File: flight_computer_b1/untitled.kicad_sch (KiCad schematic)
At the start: 1 part, among them U12 LTC7810

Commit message: WIP
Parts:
- added C12: C, symbol Device:C
- added C13: 1.2u, symbol Device:C
- added R59: 931k, symbol Device:R
- added R60: 10k, symbol Device:R
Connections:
- net V_in: now reaches U12.32 (RUN1)
- net at U12.45 (TRACK/SS1): now also C13.1
- net VFB1: now reaches U12.47 (VFB1)
- net VFB1: now also C12.2, R59.1, R60.2
- net GND: now reaches U12.9 (OVLO)
- net GND: now also C13.2, R60.1
- new net: C12.1, R59.2

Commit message: vers1
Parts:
- added C14, C15, C16, C17, C18: C, symbol Device:C
- added L2: L, symbol Device:L
- added Q3, Q4: NMOS, symbol Simulation_SPICE:NMOS
- added R62, R63: R, symbol Device:R
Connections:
- net GND: now also U12.10 (NDRV), U12.25 (PGND), U12.4 (PLLIN/SPREAD), U12.49 (SGND), U12.5 (SGND), U12.7 (REGSD), U12.8 (MODE), C16.2, C17.2, C18.1, Q4.1 (D)
- net V_in: now also C16.1, Q3.3 (S)
- net V_out: now reaches U12.1 (SENSE1-)
- net V_out: now also C15.2, C17.1, L2.1, R63.2
- net at U12.26 (DRVcc): now also C18.2
- net at U12.37 (BG1): now also Q4.2 (G)
- net at U12.40 (BOOST1): now also C14.2
- net at U12.41 (SW1): now also C14.1, L2.2, Q3.1 (D), Q4.3 (S), R62.1
- net at U12.42 (TG1): now also Q3.2 (G)
- net at U12.48 (SENSE1+): now also C15.1, R62.2, R63.1
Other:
- moved on the sheet: C12, R59, R60

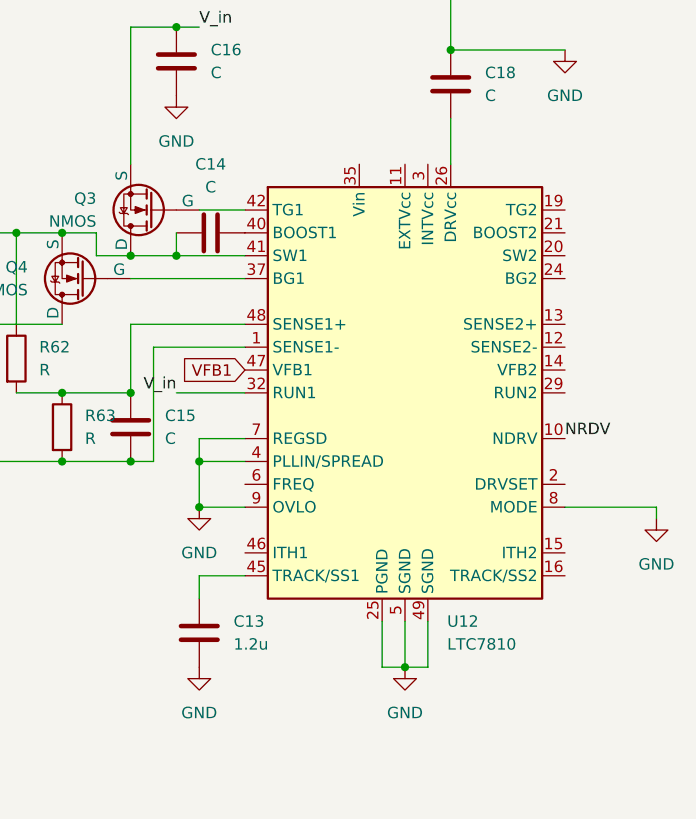
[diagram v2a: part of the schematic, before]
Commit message: Changed Schematic for LTC7801
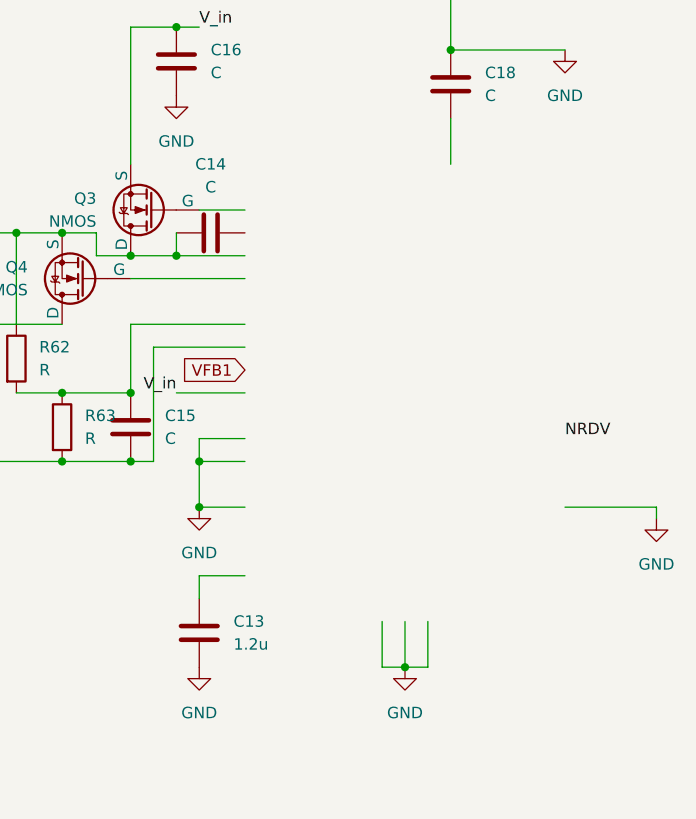
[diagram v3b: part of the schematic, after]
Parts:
- removed U12: LTC7810, Package_QFP:LQFP-48-1EP_7x7mm_P0.5mm_EP3.6x3.6mm, symbol Regulator_Controller:LTC7810
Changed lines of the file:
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@@
-	)
-	(symbol
-		(lib_id "Regulator_Controller:LTC7810")
-		(at 128.27 104.14 0)
-		(unit 1)
-		(exclude_from_sim no)
-		(in_bom yes)
-		(on_board yes)
-		(dnp no)
-		(fields_autoplaced yes)
-		(property "Reference" "U12"
-			(at 132.9533 129.54 0)
-			(effects
-				(font
-					(size 1.27 1.27)
-				)
-				(justify left)
-			)
-		)
-		(property "Value" "LTC7810"
-			(at 132.9533 132.08 0)
-			(effects
-				(font
-					(size 1.27 1.27)
-				)
-				(justify left)
-			)
-		)
-		(property "Footprint" "Package_QFP:LQFP-48-1EP_7x7mm_P0.5mm_EP3.6x3.6mm"
-			(at 137.16 128.27 0)
-			(effects
-				(font
-					(size 1.27 1.27)
-				)
-				(justify left)
-				(hide yes)
-			)
-		)
-		(property "Datasheet" "https://www.analog.com/media/en/technical-documentation/data-sheets/LTC7810.pdf"
-			(at 128.27 74.93 0)
-			(effects
-				(font
-					(size 1.27 1.27)
-				)
-				(hide yes)
-			)
-		)
-		(property "Description" "150V dual 2-phase synchronous step-down DC/DC controller, LQPF-48"
-			(at 128.27 104.14 0)
-			(effects
-				(font
-					(size 1.27 1.27)
-				)
-				(hide yes)
-			)
-		)
-		(pin "13"
-		)
-		(pin "14"
-		)
-		(pin "45"
-		)
-		(pin "26"
-		)
-		(pin "16"
-		)
-		(pin "32"
-		)
-		(pin "9"
-		)
-		(pin "35"
-		)
-		(pin "3"
-		)
-		(pin "40"
-		)
-		(pin "19"
-		)
-		(pin "24"
-		)
-		(pin "41"
-		)
-		(pin "1"
-		)
-		(pin "37"
-		)
-		(pin "47"
-		)
-		(pin "42"
-		)
-		(pin "7"
-		)
-		(pin "46"
-		)
-		(pin "25"
-		)
-		(pin "48"
-		)
-		(pin "4"
-		)
-		(pin "6"
-		)
-		(pin "11"
-		)
-		(pin "5"
-		)
-		(pin "49"
-		)
-		(pin "21"
-		)
-		(pin "20"
-		)
-		(pin "12"
-		)
-		(pin "29"
-		)
-		(pin "10"
-		)
-		(pin "2"
-		)
-		(pin "8"
-		)
-		(pin "15"
-		)
-		(instances
-			(project ""
-				(path "/b71a7b79-cdb5-4e38-a72c-0daaa3474f05/dafce160-673b-4056-acfb-f0ec341d8d32"
-					(reference "U12")
-					(unit 1)
-				)
-			)
-		)
 	)
 	(symbol

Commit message: Fixed Schematic
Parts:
- added U12: LTC7801IFE-TRPBF, FE_24_ADI, symbol LTC7801:LTC7801IFE-TRPBF
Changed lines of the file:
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@@
+	)
+	(symbol
+		(lib_id "LTC7801:LTC7801IFE-TRPBF")
+		(at 167.64 77.47 0)
+		(unit 1)
+		(exclude_from_sim no)
+		(in_bom yes)
+		(on_board yes)
+		(dnp no)
+		(fields_autoplaced yes)
+		(property "Reference" "U12"
+			(at 193.04 67.31 0)
+			(effects
+				(font
+					(size 1.524 1.524)
+				)
+			)
+		)
+		(property "Value" "LTC7801IFE-TRPBF"
+			(at 193.04 69.85 0)
+			(effects
+				(font
+					(size 1.524 1.524)
+				)
+			)
+		)
+		(property "Footprint" "FE_24_ADI"
+			(at 167.64 77.47 0)
+			(effects
+				(font
+					(size 1.27 1.27)
+					(italic yes)
+				)
+				(hide yes)
+			)
+		)
+		(property "Datasheet" "https://www.analog.com/media/en/technical-documentation/data-sheets/ltc7801.pdf"
+			(at 167.64 77.47 0)
+			(effects
+				(font
+					(size 1.27 1.27)
+					(italic yes)
+				)
+				(hide yes)
+			)
+		)
+		(property "Description" ""
+			(at 167.64 77.47 0)
+			(effects
+				(font
+					(size 1.27 1.27)
+				)
+				(hide yes)
+			)
+		)
+		(pin "1"
+		)
+		(pin "14"
+		)
+		(pin "13"
+		)
+		(pin "17"
+		)
+		(pin "16"
+		)
+		(pin "15"
+		)
+		(pin "20"
+		)
+		(pin "19"
+		)
+		(pin "18"
+		)
+		(pin "23"
+		)
+		(pin "22"
+		)
+		(pin "21"
+		)
+		(pin "10"
+		)
+		(pin "11"
+		)
+		(pin "12"
+		)
+		(pin "EPAD"
+		)
+		(pin "24"
+		)
+		(pin "3"
+		)
+		(pin "4"
+		)
+		(pin "5"
+		)
+		(pin "6"
+		)
+		(pin "7"
+		)
+		(pin "8"
+		)
+		(pin "9"
+		)
+		(pin "2"
+		)
+		(instances
+			(project ""
+				(path "/b71a7b79-cdb5-4e38-a72c-0daaa3474f05/dafce160-673b-4056-acfb-f0ec341d8d32"
+					(reference "U12")
+					(unit 1)
+				)
+			)
+		)
 	)
 	(symbol

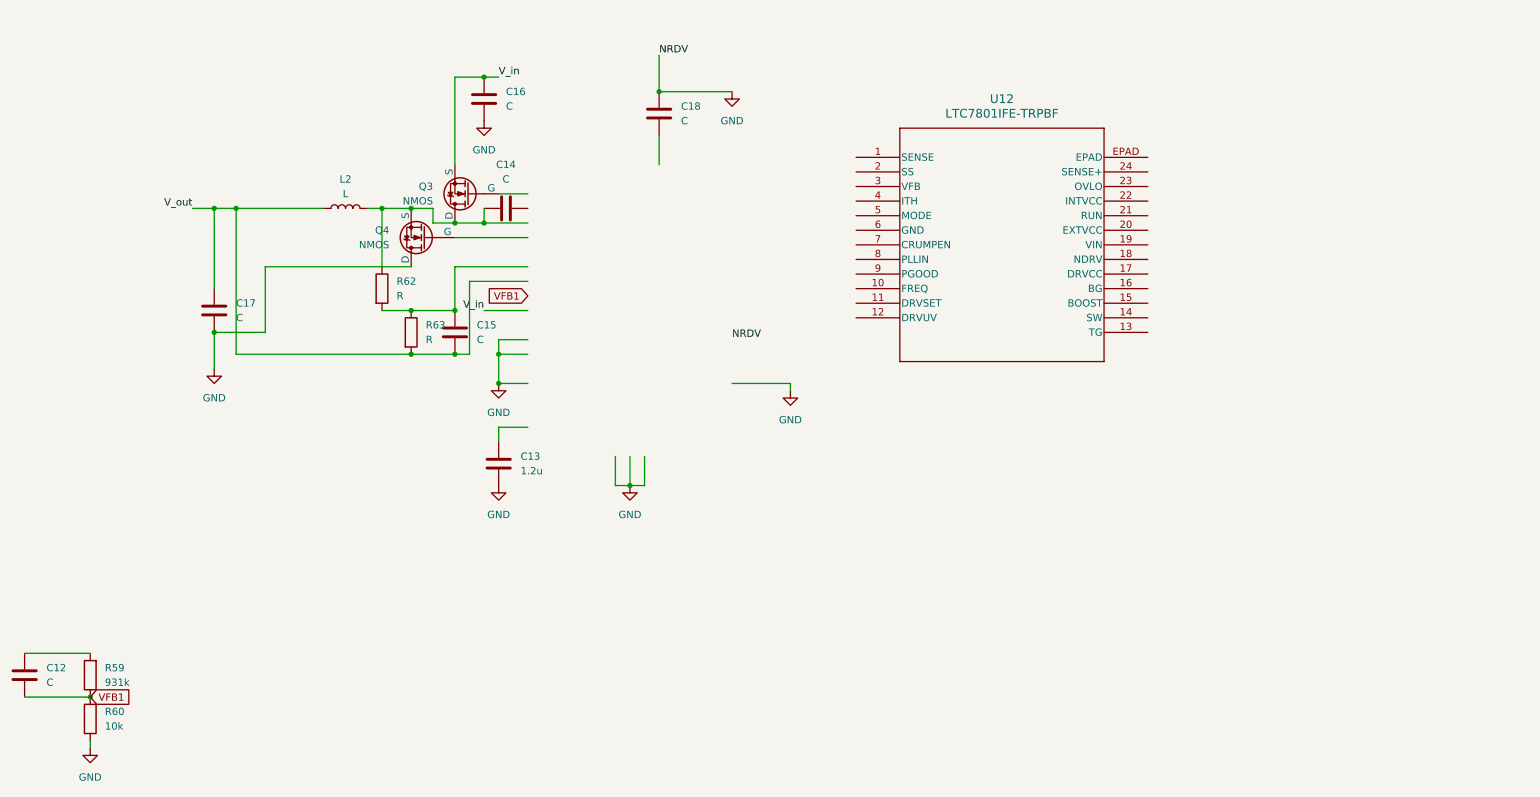
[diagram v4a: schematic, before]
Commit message: Final
Fixed symbol error and created functional schematic instead.
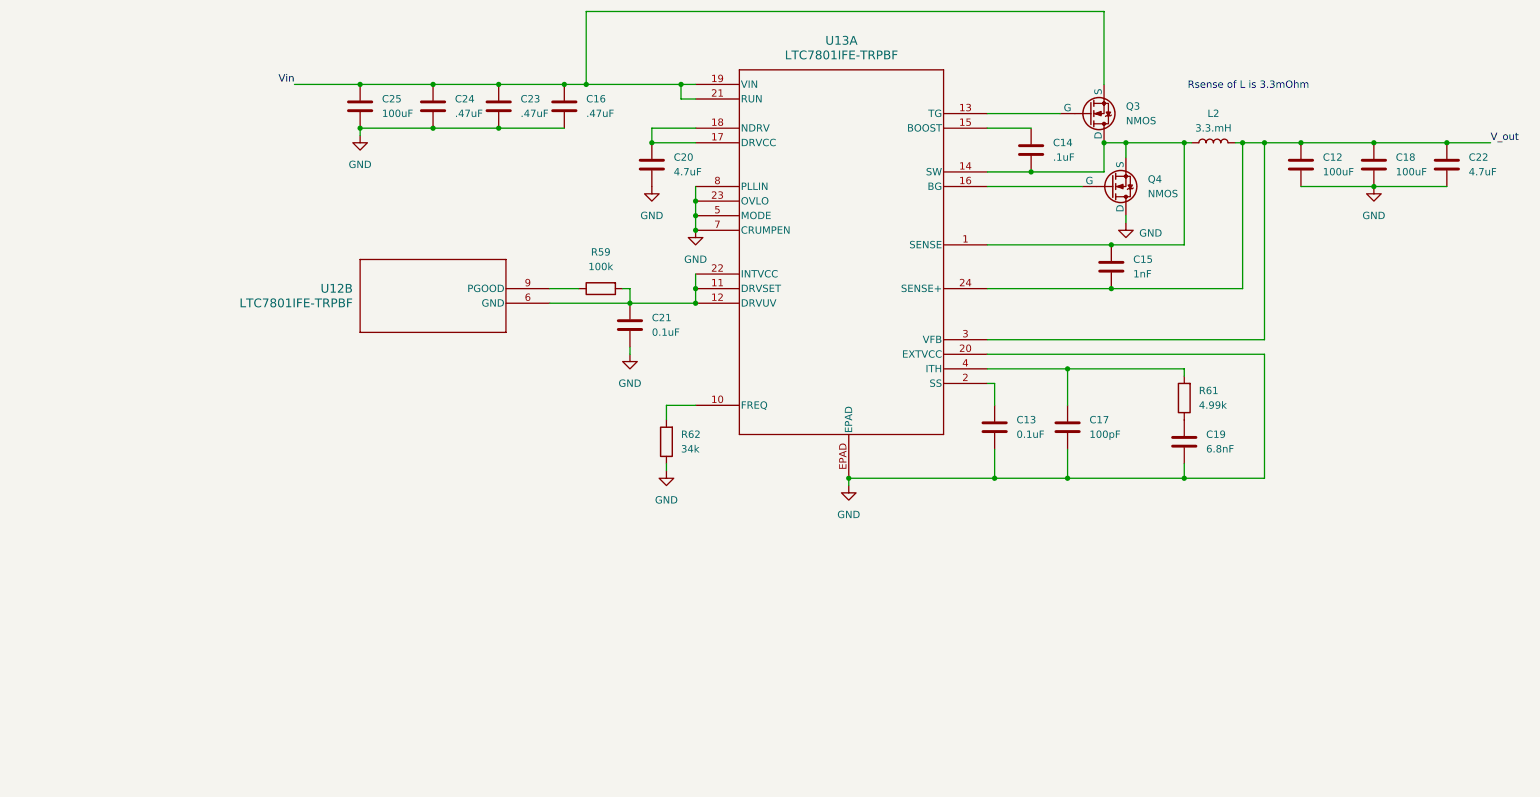
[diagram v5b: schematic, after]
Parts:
- removed R60: 10k, symbol Device:R
- removed R63: R, symbol Device:R
- removed U12: LTC7801IFE-TRPBF, FE_24_ADI, symbol LTC7801:LTC7801IFE-TRPBF
- added C19: 6.8nF, symbol Device:C
- added C20, C22: 4.7uF, symbol Device:C
- added C21: 0.1uF, symbol Device:C
- added C23, C24: .47uF, symbol Device:C
- added C25: 100uF, symbol Device:C
- added R61: 4.99k, symbol Device:R
- added U12, U13: LTC7801IFE-TRPBF, FE_24_ADI, symbol LTC7801:LTC7801IFE-TRPBF
- C12, C18: value C -> 100uF
- C13: value 1.2u -> 0.1uF
- C14: value C -> .1uF
- C15: value C -> 1nF
- C16: value C -> .47uF
- C17: value C -> 100pF
- L2: value L -> 3.3.mH
- R59: value 931k -> 100k
- R62: value R -> 34k
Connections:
- net GND: now also C12.2, C18.2, R62.1, C19.2, C20.2, C21.2, C22.2, C23.2, C24.2, C25.2, U13.20 (EXTVCC), U13.23 (OVLO), U13.5 (MODE), U13.7 (CRUMPEN), U13.8 (PLLIN), U13.EPAD; no longer C18.1
- net V_out: now also C12.1, C18.1, C22.1, U13.24 (SENSE+), U13.3 (VFB); no longer C17.1
- net at C13.1: now also U13.2 (SS)
- net at R59.2: now also C21.1, U12.6 (GND), U13.11 (DRVSET), U13.12 (DRVUV), U13.22 (INTVCC); no longer C12.1
- net at R62.2: now also U13.10 (FREQ); no longer C15.1
- net at L2.2, Q3.1 (D), Q4.3 (S): now also C14.2, C15.1, U13.1 (SENSE), U13.14 (SW); no longer C14.1, R62.1
- net at Q4.2 (G): now also U13.16 (BG)
- net at Q3.2 (G): now also U13.13 (TG)
- net VFB1: no longer names the net of R59.1
- net VFB1: now also U12.9 (PGOOD); no longer C12.2
- net V_in renamed Vin
- net Vin: now also C23.1, C24.1, C25.1, U13.19 (VIN), U13.21 (RUN)
- new net: C14.1, U13.15 (BOOST)
- new net: C19.1, R61.1
- new net: C17.1, R61.2, U13.4 (ITH)
- new net: C20.1, U13.17 (DRVCC), U13.18 (NDRV)
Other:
- note added: "Rsense of L is 3.3mOhm"
- moved on the sheet: C14, C15, C16, L2, Q3, Q4
